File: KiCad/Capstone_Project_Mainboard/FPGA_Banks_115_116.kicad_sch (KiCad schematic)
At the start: 2 parts, among them U1 XC7K160T-FFG676_MIB

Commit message: Updated FPGA Footprint
Added die-to-pad length offsets to all pins of the FFG676 package. These values were derived from the delay files provided in Vivado.
+ Other minor bugfixes
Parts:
- U1: footprint Capstone_Library:Xilinx_FFG676_MOD -> Capstone_Library:Xilinx_FFG676_K7_160T
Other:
- note added: "<- Add ref clk here"
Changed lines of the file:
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@@
   (title_block
     (title "FPGA Banks 115 & 116 (GTX) I/O")
-    (date "2023-12-18")
+    (date "2023-12-22")
     (rev "A")
     (company "Jordan Harris-Toovy")
@@
     (at 26.67 38.735 0)
     (effects (font (size 1.27 1.27) (thickness 0.254) bold (color 185 1 8 1)) (justify left bottom))
+  )
+  (text "<- Add ref clk here" (at 140.97 72.39 0)
+    (effects (font (size 1.27 1.27) (thickness 0.254) bold) (justify left bottom))
   )
   (symbol (lib_id "Capstone_Library:XC7K160T-FFG676_MIB") (at 109.22 22.86 0) (unit 10)
@@
       (effects (font (size 1.27 1.27)) (justify right))
     )
-    (property "Footprint" "Capstone_Library:Xilinx_FFG676_MOD" (at 107.95 19.05 0)
+    (property "Footprint" "Capstone_Library:Xilinx_FFG676_K7_160T" (at 107.95 19.05 0)
       (effects (font (size 1.27 1.27)) hide)
     )
@@
       (effects (font (size 1.27 1.27)) (justify right))
     )
-    (property "Footprint" "Capstone_Library:Xilinx_FFG676_MOD" (at 107.95 88.9 0)
+    (property "Footprint" "Capstone_Library:Xilinx_FFG676_K7_160T" (at 107.95 88.9 0)
       (effects (font (size 1.27 1.27)) hide)
     )

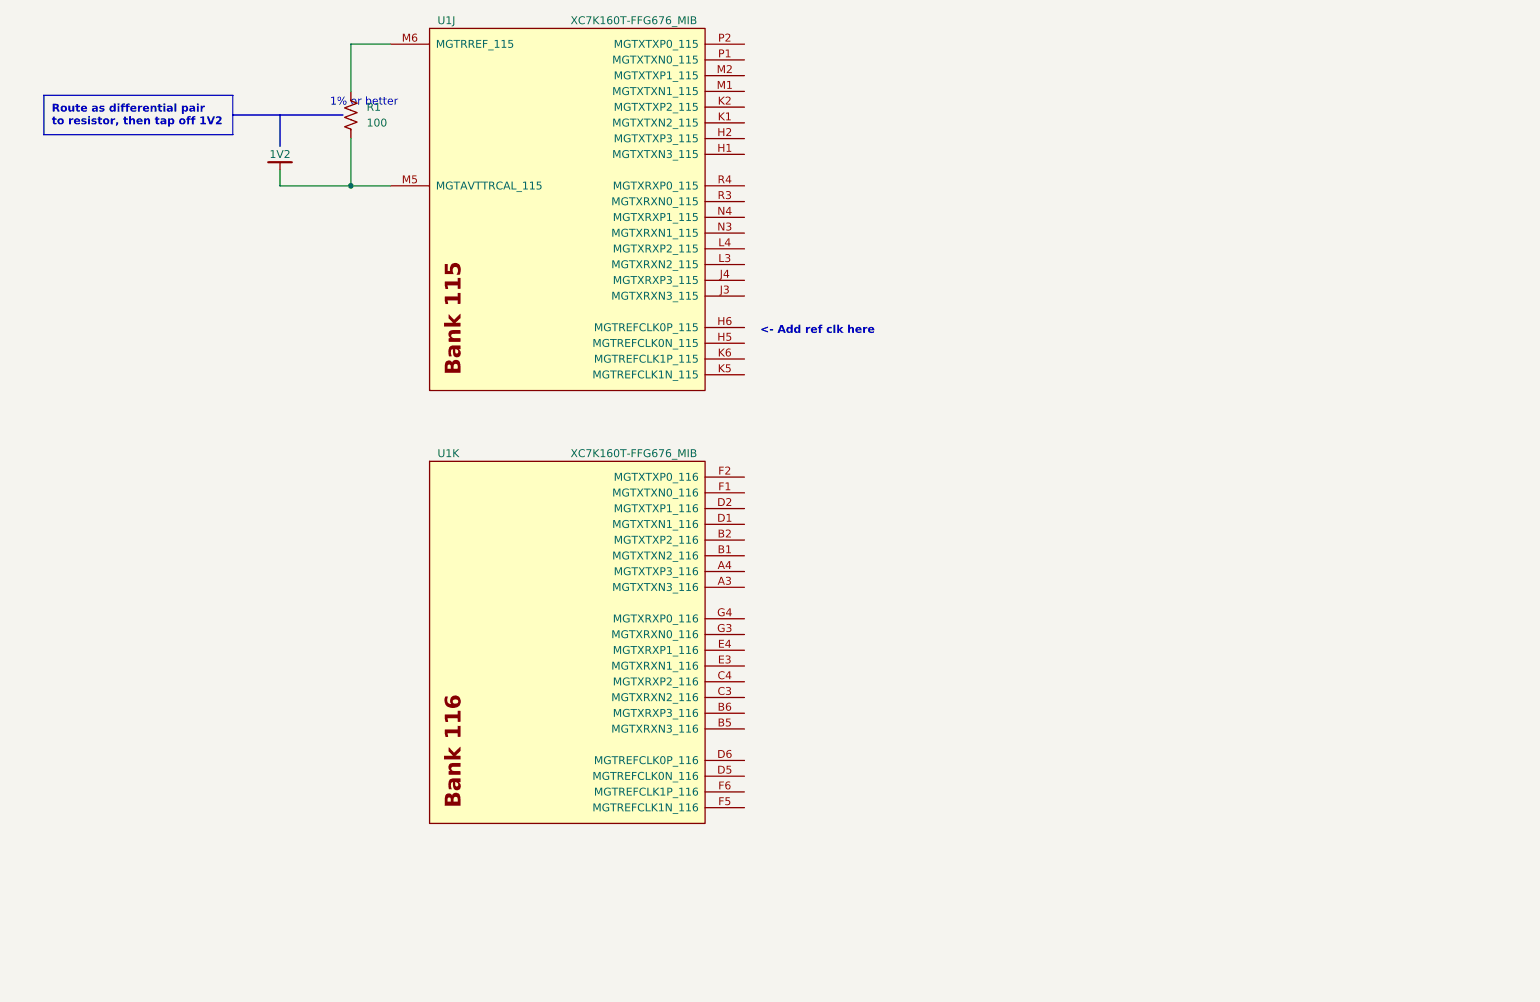
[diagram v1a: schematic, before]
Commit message: Core non-power parts defined
Most major non-power components added to KiCad project
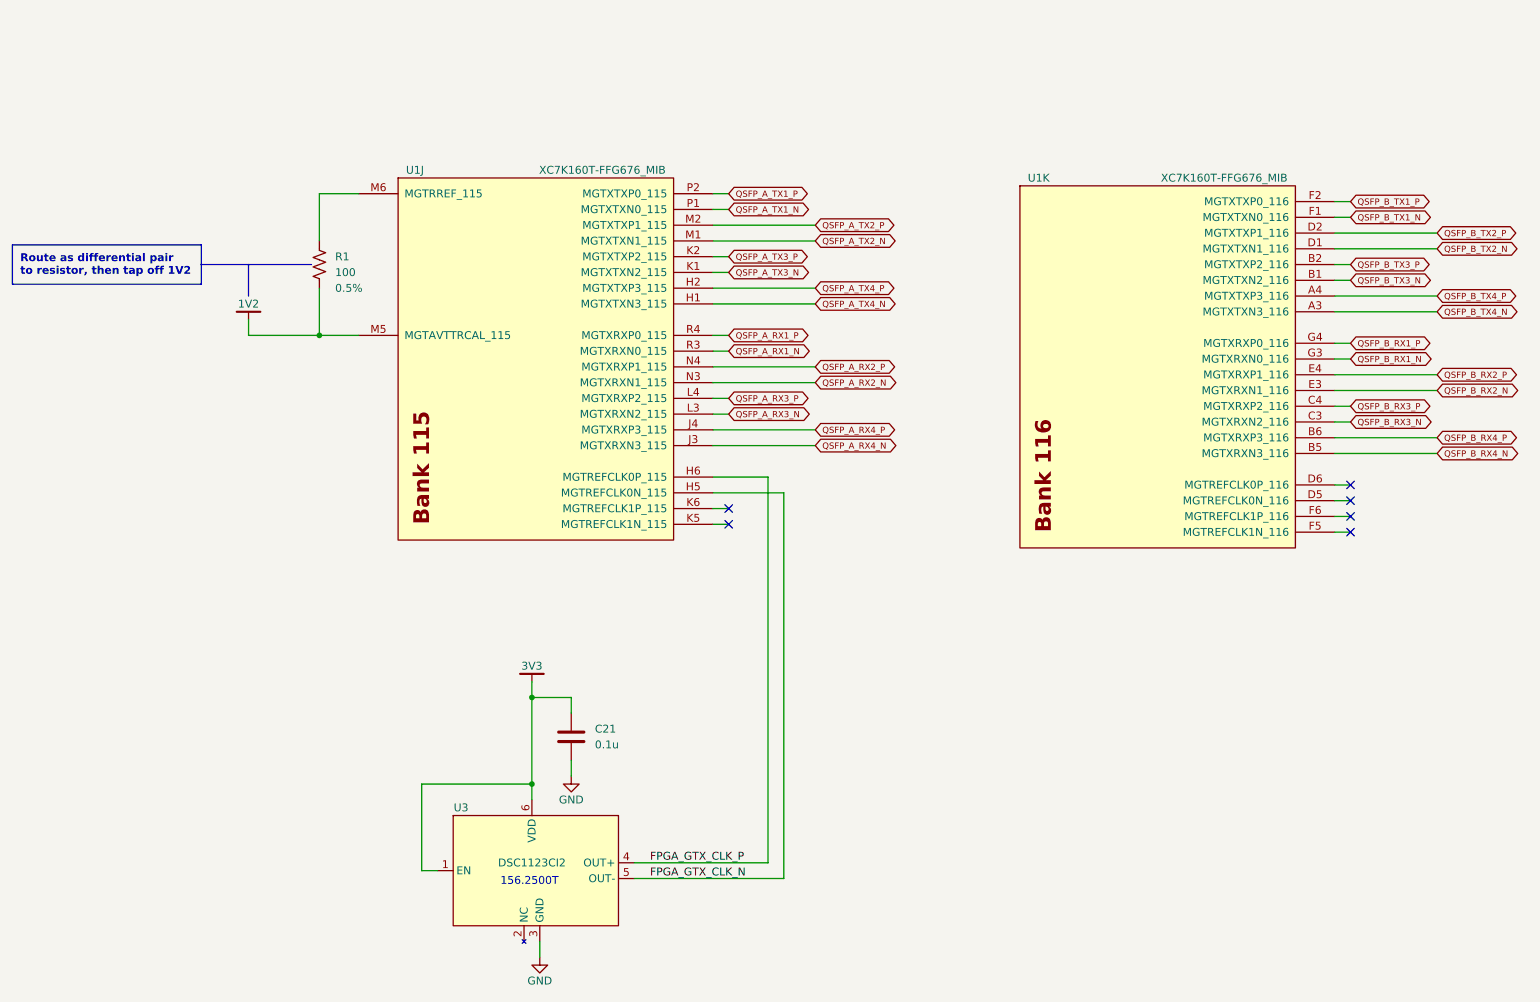
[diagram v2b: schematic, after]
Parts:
- added C21: 0.1u, Capacitor_SMD:C_0402_1005Metric, symbol Device:C
- added U3: DSC1123CI2, Capstone_Library:Microchip_6-VDFN, symbol Capstone_Library:DSC1123C
- R1: footprint (none) -> Resistor_SMD:R_0402_1005Metric; Notes (none) -> 0.5%; Part Number (none) -> MCS0402PD1000DE500
- U1: Part Number (none) -> XC7K160T-2FFG676I
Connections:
- net QSFP_A_TX4_N: now reaches U1.H1 (MGTXTXN3_115)
- net QSFP_A_TX4_P: now reaches U1.H2 (MGTXTXP3_115)
- net FPGA_GTX_CLK_N: now reaches U1.H5 (MGTREFCLK0N_115)
- net FPGA_GTX_CLK_N: now also U3.5 (OUT-)
- net FPGA_GTX_CLK_P: now reaches U1.H6 (MGTREFCLK0P_115)
- net FPGA_GTX_CLK_P: now also U3.4 (OUT+)
- net QSFP_A_RX4_N: now reaches U1.J3 (MGTXRXN3_115)
- net QSFP_A_RX4_P: now reaches U1.J4 (MGTXRXP3_115)
- net QSFP_A_TX3_N: now reaches U1.K1 (MGTXTXN2_115)
- net QSFP_A_TX3_P: now reaches U1.K2 (MGTXTXP2_115)
- net QSFP_A_RX3_N: now reaches U1.L3 (MGTXRXN2_115)
- net QSFP_A_RX3_P: now reaches U1.L4 (MGTXRXP2_115)
- net QSFP_A_TX2_N: now reaches U1.M1 (MGTXTXN1_115)
- net QSFP_A_TX2_P: now reaches U1.M2 (MGTXTXP1_115)
- net QSFP_A_RX2_N: now reaches U1.N3 (MGTXRXN1_115)
- net QSFP_A_RX2_P: now reaches U1.N4 (MGTXRXP1_115)
- net QSFP_A_TX1_N: now reaches U1.P1 (MGTXTXN0_115)
- net QSFP_A_TX1_P: now reaches U1.P2 (MGTXTXP0_115)
- net QSFP_A_RX1_N: now reaches U1.R3 (MGTXRXN0_115)
- net QSFP_A_RX1_P: now reaches U1.R4 (MGTXRXP0_115)
- net QSFP_B_TX4_N: now reaches U1.A3 (MGTXTXN3_116)
- net QSFP_B_TX4_P: now reaches U1.A4 (MGTXTXP3_116)
- net QSFP_B_TX3_N: now reaches U1.B1 (MGTXTXN2_116)
- net QSFP_B_TX3_P: now reaches U1.B2 (MGTXTXP2_116)
- net QSFP_B_RX4_N: now reaches U1.B5 (MGTXRXN3_116)
- net QSFP_B_RX4_P: now reaches U1.B6 (MGTXRXP3_116)
- net QSFP_B_RX3_N: now reaches U1.C3 (MGTXRXN2_116)
- net QSFP_B_RX3_P: now reaches U1.C4 (MGTXRXP2_116)
- net QSFP_B_TX2_N: now reaches U1.D1 (MGTXTXN1_116)
- net QSFP_B_TX2_P: now reaches U1.D2 (MGTXTXP1_116)
- net QSFP_B_RX2_N: now reaches U1.E3 (MGTXRXN1_116)
- net QSFP_B_RX2_P: now reaches U1.E4 (MGTXRXP1_116)
- net QSFP_B_TX1_N: now reaches U1.F1 (MGTXTXN0_116)
- net QSFP_B_TX1_P: now reaches U1.F2 (MGTXTXP0_116)
- net QSFP_B_RX1_N: now reaches U1.G3 (MGTXRXN0_116)
- net QSFP_B_RX1_P: now reaches U1.G4 (MGTXRXP0_116)
- new net 3V3: C21.1, U3.1 (EN), U3.6 (VDD)
- new net GND: C21.2, U3.3 (GND)
- no-connect marks 0 -> 6
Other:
- note added: "156.2500T"
- note removed: "1% or better"
- note removed: "<- Add ref clk here"
- title: FPGA Banks 115 & 116 (GTX) I/O -> FPGA Banks 115 & 116 (GTX) I/O + SFI Clock
- moved on the sheet: R1, U1J, U1K
